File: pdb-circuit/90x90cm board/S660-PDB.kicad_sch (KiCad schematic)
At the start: 45 parts, among them J1 PWR INPUT, J2 PWR OUTPUT, J3 JST-XH 6p to Pi, K1 G2RL-1A DC12, Q2 BC337-40, Q3 2N7000, U1 ATtiny85-20P, U2 LM2936Z-3.3, U3 PC817

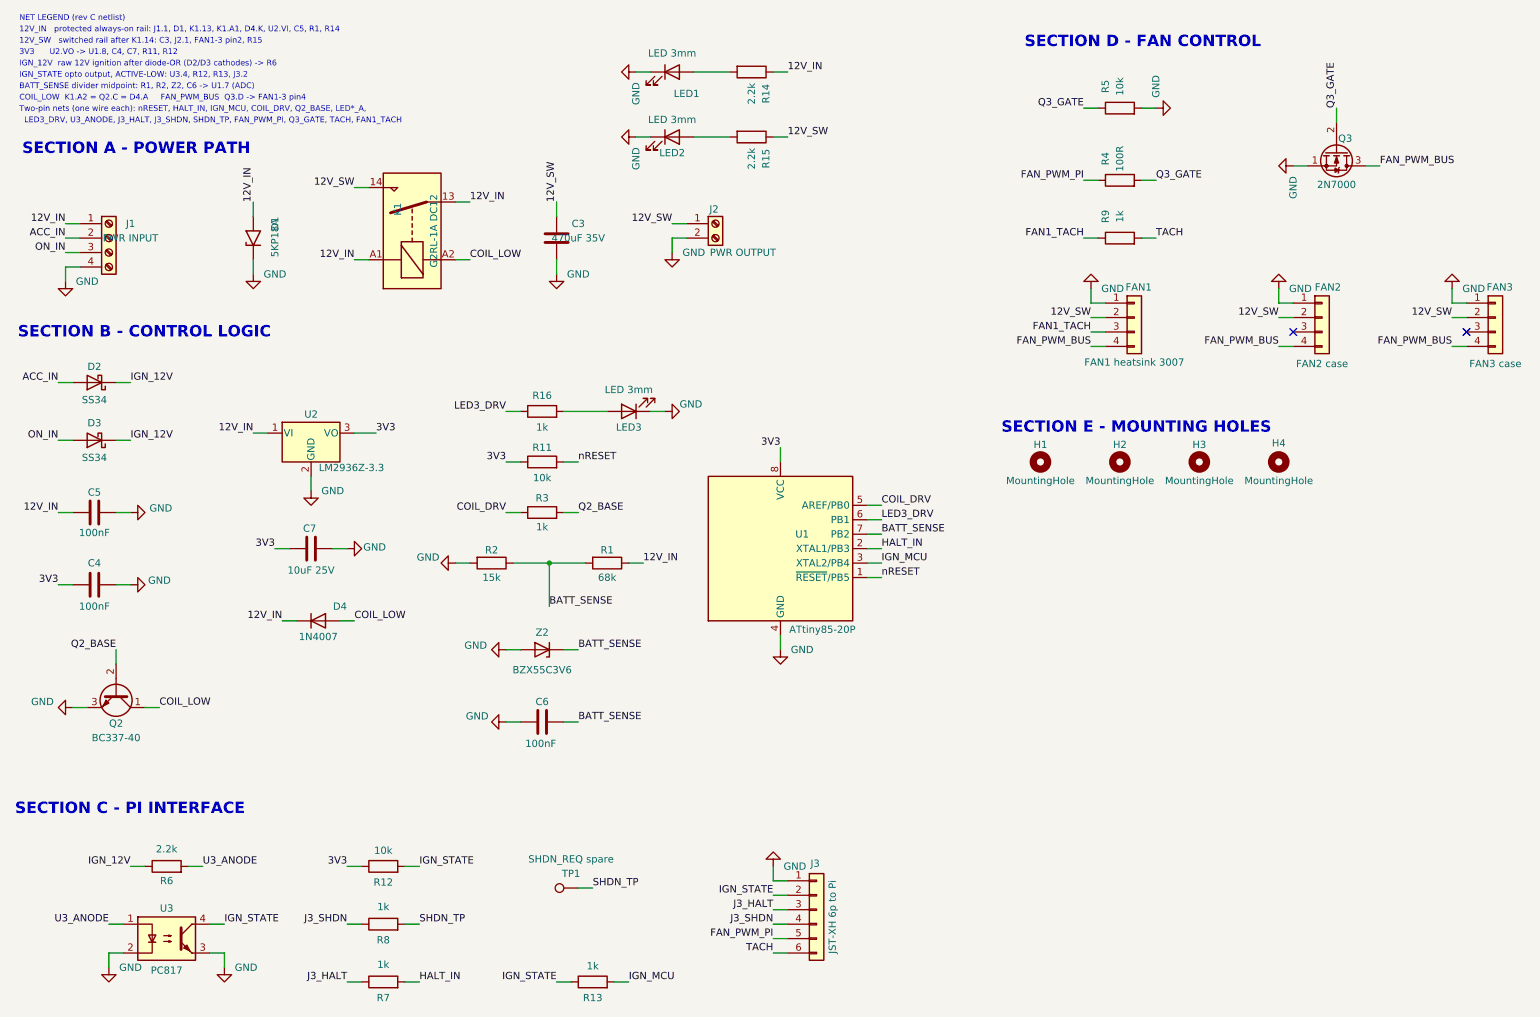
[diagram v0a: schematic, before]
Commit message: PDB rev D: schematic/PCB updates, review notes, BOM/CPL, gerbers and assembly package
Co-Authored-By: Claude Opus 5.5 <noreply@anthropic.com>
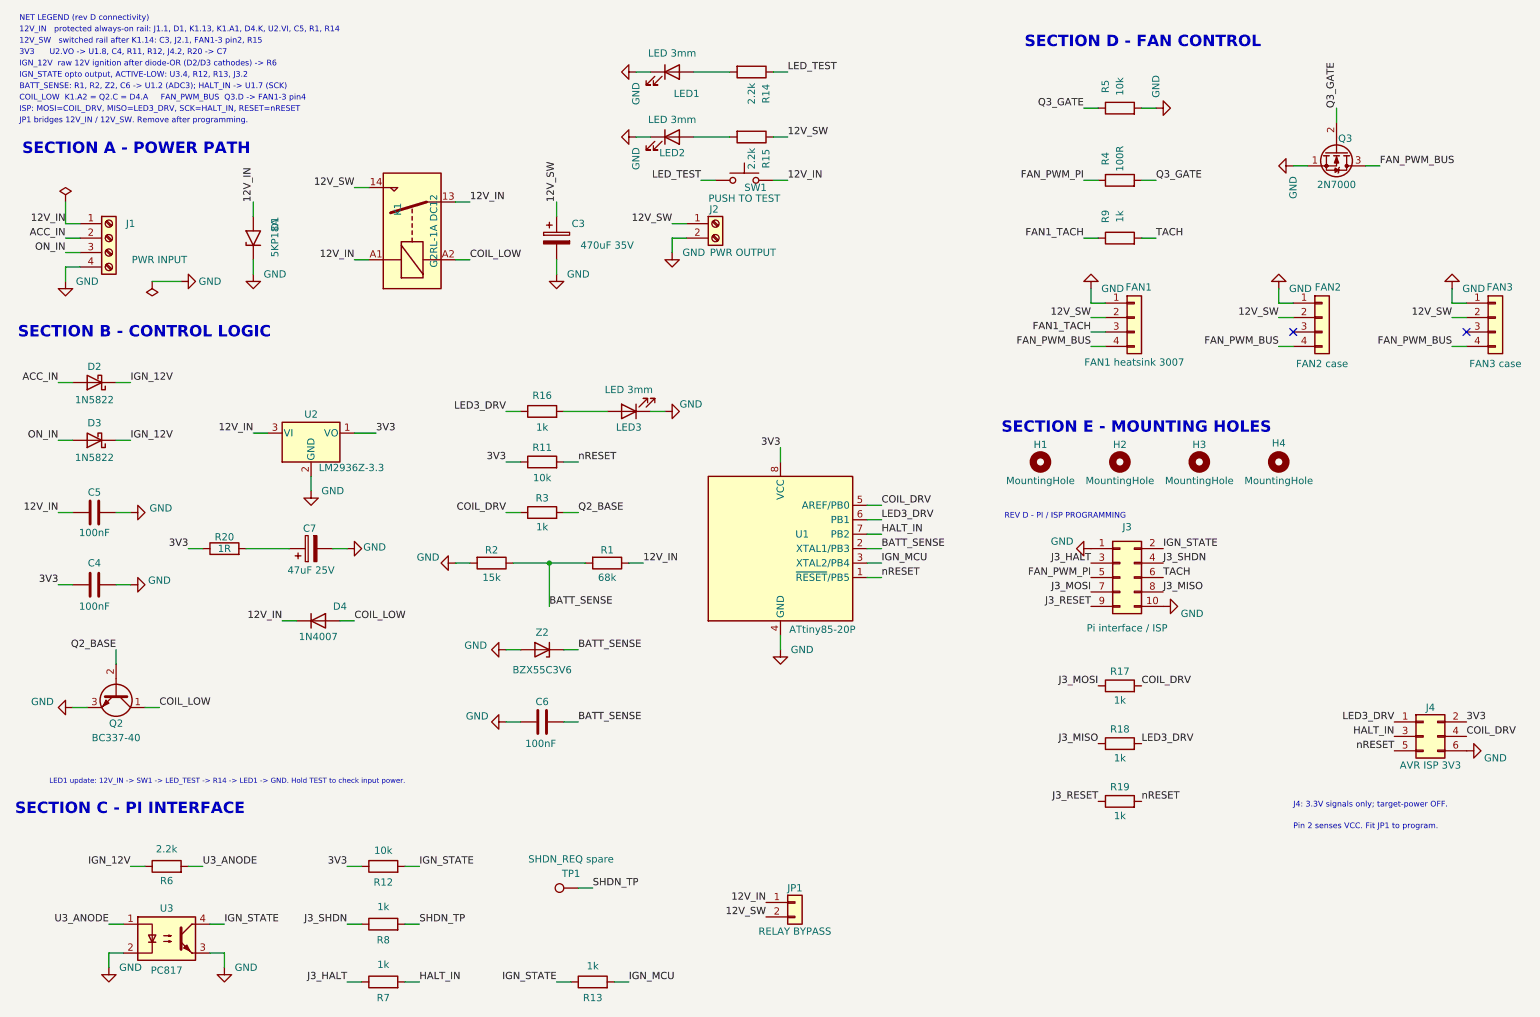
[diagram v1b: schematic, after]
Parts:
- added J4: AVR ISP 3V3, Connector_PinHeader_2.54mm:PinHeader_2x03_P2.54mm_Vertical, symbol Connector_Generic:Conn_02x03_Odd_Even
- added JP1: RELAY BYPASS, S660-PDB:Phoenix_MKDS_1_2_3.5_1751248, symbol Connector_Generic:Conn_01x02
- added R17, R18, R19: 1k, Resistor_THT:R_Axial_DIN0207_L6.3mm_D2.5mm_P10.16mm_Horizontal, symbol Device:R
- added R20: 1R, Resistor_THT:R_Axial_DIN0207_L6.3mm_D2.5mm_P10.16mm_Horizontal, symbol Device:R
- added SW1: PUSH TO TEST, Button_Switch_THT:SW_PUSH_6mm_H4.3mm, symbol Switch:SW_Push
- C3: symbol Device:C -> Device:C_Polarized; Assembly LCSC (none) -> C178715; Assembly MPN (none) -> EEUFR1V471; Assembly Manufacturer (none) -> Panasonic; Assembly Notes (none) -> 10 mm diameter; 5 mm lead pitch. Do not substitute EEUFR1V4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; LCSC (none) -> C178715; MPN (none) -> EEUFR1V471; Manufacturer (none) -> Panasonic
- C4, C5, C6: Assembly LCSC (none) -> C448595; Assembly MPN (none) -> FG28X7R1H104KNT00; Assembly Manufacturer (none) -> TDK; Assembly Notes (none) -> 100 nF 50 V X7R 10%; radial 5 mm pitch.; LCSC (none) -> C448595; MPN (none) -> FG28X7R1H104KNT00; Manufacturer (none) -> TDK
- C7: value 10uF 25V -> 47uF 25V; symbol Device:C -> Device:C_Polarized; Assembly LCSC (none) -> C407893; Assembly MPN (none) -> EEUFR1E470; Assembly Manufacturer (none) -> Panasonic; LCSC (none) -> C407893; MPN (none) -> EEUFR1E470; Manufacturer (none) -> Panasonic; Selection requirement (none) -> EEUFR1E470 with R20=1 ohm in series; validate effective C>=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
- D1: Assembly MPN (none) -> 5KP18A; Assembly Manufacturer (none) -> Diotec Semiconductor; MPN (none) -> 5KP18A; Manufacturer (none) -> Diotec Semiconductor
- D2, D3: value SS34 -> 1N5822; footprint Diode_THT:D_DO-41_SOD81_P10.16mm_Horizontal -> S660-PDB:D_Multicomp_1N5822_DO27_P15.24mm; symbol Diode:SS34 -> Diode:1N5822; Assembly MPN (none) -> 1N5822; Assembly Manufacturer (none) -> Multicomp Pro; Assembly Notes (none) -> Exact Farnell 4050109 DO-27 package; do not substitute DO-2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; Farnell (none) -> 4050109; MPN (none) -> 1N5822; Manufacturer (none) -> Multicomp Pro
- D4: Assembly MPN (none) -> 1N4007-E3/54; Assembly Manufacturer (none) -> Vishay; MPN (none) -> 1N4007-E3/54; Manufacturer (none) -> Vishay
- FAN1, FAN2, FAN3: Assembly MPN (none) -> TSW-104-07-G-S; Assembly Manufacturer (none) -> Samtec; Assembly Notes (none) -> Fit male 1x4 header, not a fan. Verify finished-hole fit wi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; MPN (none) -> TSW-104-07-G-S; Manufacturer (none) -> Samtec
- J1: footprint Connector_Phoenix_MC_HighVoltage:PhoenixContact_MC_1,5_4-GF-5.08_1x04_P5.08mm_Horizontal_ThreadedFlange -> Connector_Phoenix_MC_HighVoltage:PhoenixContact_MC_1,5_4-G-5.08_1x04_P5.08mm_Horizontal; Assembly LCSC (none) -> C5444352; Assembly MPN (none) -> 1836202; Assembly Manufacturer (none) -> Phoenix Contact; Assembly Notes (none) -> PCB header only; mating cable plug not included.; LCSC (none) -> C5444352; MPN (none) -> 1836202; Manufacturer (none) -> Phoenix Contact
- J2: footprint Connector_Phoenix_MC_HighVoltage:PhoenixContact_MC_1,5_2-GF-5.08_1x02_P5.08mm_Horizontal_ThreadedFlange -> Connector_Phoenix_MC_HighVoltage:PhoenixContact_MC_1,5_2-G-5.08_1x02_P5.08mm_Horizontal; Assembly LCSC (none) -> C5355140; Assembly MPN (none) -> 1836189; Assembly Manufacturer (none) -> Phoenix Contact; Assembly Notes (none) -> PCB header only; mating cable plug not included.; LCSC (none) -> C5355140; MPN (none) -> 1836189; Manufacturer (none) -> Phoenix Contact
- J3: value JST-XH 6p to Pi -> Pi interface / ISP; footprint Connector_JST:JST_XH_B6B-XH-A_1x06_P2.50mm_Vertical -> Connector_PinHeader_2.54mm:PinHeader_2x05_P2.54mm_Vertical; symbol Connector_Generic:Conn_01x06 -> Connector_Generic:Conn_02x05_Odd_Even; Assembly MPN (none) -> TSW-105-07-G-D; Assembly Manufacturer (none) -> Samtec; Assembly Notes (none) -> Male 2x5 header; verify finished-hole fit with assembler.; MPN (none) -> TSW-105-07-G-D; Manufacturer (none) -> Samtec
- K1: Assembly LCSC (none) -> C1524657; Assembly MPN (none) -> G2RL-1A DC12; Assembly Manufacturer (none) -> Omron; LCSC (none) -> C1524657; MPN (none) -> G2RL-1A DC12; Manufacturer (none) -> Omron
- LED1, LED2, LED3: Assembly MPN (none) -> WP3A8ID; Assembly Manufacturer (none) -> Kingbright; Assembly Notes (none) -> Red 3 mm LED; pad 1 cathode.; MPN (none) -> WP3A8ID; Manufacturer (none) -> Kingbright
- Q2: footprint Package_TO_SOT_THT:TO-92_Inline -> Package_TO_SOT_THT:TO-92_Inline_Wide; Assembly MPN (none) -> BC337-40; Assembly Manufacturer (none) -> Diotec Semiconductor; Assembly Notes (none) -> Pads 1 C, 2 B, 3 E. 2.54 mm pitch; confirm lead forming.; MPN (none) -> BC337-40; Manufacturer (none) -> Diotec Semiconductor
- Q3: footprint Package_TO_SOT_THT:TO-92_Inline -> Package_TO_SOT_THT:TO-92_Inline_Wide; Assembly MPN (none) -> 2N7000; Assembly Manufacturer (none) -> Diotec Semiconductor; Assembly Notes (none) -> Pads 1 S, 2 G, 3 D. 2.54 mm pitch.; MPN (none) -> 2N7000; Manufacturer (none) -> Diotec Semiconductor
- R1: Assembly MPN (none) -> MFR-25FBF52-68K; Assembly Manufacturer (none) -> Yageo; Assembly Notes (none) -> 1%, 0.25 W; form axial leads to 10.16 mm.; MPN (none) -> MFR-25FBF52-68K; Manufacturer (none) -> Yageo
- R11, R12, R5: Assembly LCSC (none) -> C1519255; Assembly MPN (none) -> MFR-25FBF52-10K; Assembly Manufacturer (none) -> Yageo; Assembly Notes (none) -> 1%, 0.25 W; form axial leads to 10.16 mm.; LCSC (none) -> C1519255; MPN (none) -> MFR-25FBF52-10K; Manufacturer (none) -> Yageo
- R13, R16, R3, R7, R8, R9: Assembly LCSC (none) -> C1364484; Assembly MPN (none) -> MFR-25FBF52-1K; Assembly Manufacturer (none) -> Yageo; Assembly Notes (none) -> 1%, 0.25 W; form axial leads to 10.16 mm.; LCSC (none) -> C1364484; MPN (none) -> MFR-25FBF52-1K; Manufacturer (none) -> Yageo
- R14, R15, R6: Assembly MPN (none) -> MFR-25FBF52-2K2; Assembly Manufacturer (none) -> Yageo; Assembly Notes (none) -> 1%, 0.25 W; form axial leads to 10.16 mm.; MPN (none) -> MFR-25FBF52-2K2; Manufacturer (none) -> Yageo
- R2: Assembly LCSC (none) -> C3556390; Assembly MPN (none) -> MFR-25FBF52-15K; Assembly Manufacturer (none) -> Yageo; Assembly Notes (none) -> 1%, 0.25 W; form axial leads to 10.16 mm.; LCSC (none) -> C3556390; MPN (none) -> MFR-25FBF52-15K; Manufacturer (none) -> Yageo
- R4: Assembly MPN (none) -> MFR-25FBF52-100R; Assembly Manufacturer (none) -> Yageo; Assembly Notes (none) -> 1%, 0.25 W; form axial leads to 10.16 mm.; MPN (none) -> MFR-25FBF52-100R; Manufacturer (none) -> Yageo
- U1: Assembly LCSC (none) -> C3170386; Assembly MPN (none) -> A 08-LC-TT; Assembly Manufacturer (none) -> ASSMANN WSW Components; Assembly Notes (none) -> ASSEMBLY OVERRIDE: fit socket only; owner inserts ATtiny85.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; LCSC (none) -> C965497; MPN (none) -> ATTINY85-20PU; Manufacturer (none) -> Microchip; Socket Datasheet (none) -> https://www.assmann-wsw.com/uploads/datasheets/ASS_0810_CO.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
- U2: footprint Package_TO_SOT_THT:TO-92_Inline -> Package_TO_SOT_THT:TO-92_Inline_Wide; symbol Regulator_Linear:LM2936-3.3 -> Regulator_Linear:LM2936-3.3_TO92; Assembly MPN (none) -> LM2936Z-3.3/NOPB; Assembly Manufacturer (none) -> Texas Instruments; Assembly Notes (none) -> 3.3 V variant only; pads 1 OUT, 2 GND, 3 IN. Form leads to 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; MPN (none) -> LM2936Z-3.3/NOPB; Manufacturer (none) -> Texas Instruments
- U3: Assembly MPN (none) -> ISP817X; Assembly Manufacturer (none) -> Isocom Components; Assembly Notes (none) -> DIP-4 7.62 mm; pads 1 A, 2 K, 3 E, 4 C.; MPN (none) -> ISP817X; Manufacturer (none) -> Isocom Components
- Z2: Assembly MPN (none) -> BZX55C3V6-TAP; Assembly Manufacturer (none) -> Vishay; MPN (none) -> BZX55C3V6-TAP; Manufacturer (none) -> Vishay
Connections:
- net 12V_IN: now also U2.3 (VI), JP1.1 (Pin_1), SW1.2; no longer R14.1, U2.1 (VI)
- net 12V_SW: now also JP1.2 (Pin_2)
- net 3V3: now also U2.1 (VO), J4.2 (Pin_2), R20.1; no longer C7.1, U2.3 (VO)
- net BATT_SENSE: now also U1.2 (XTAL1/PB3); no longer U1.7 (PB2)
- net COIL_DRV: now also J4.4 (Pin_4), R17.2
- net GND: now also J3.10 (Pin_10), J4.6 (Pin_6)
- net HALT_IN: now also U1.7 (PB2), J4.3 (Pin_3); no longer U1.2 (XTAL1/PB3)
- net LED3_DRV: now also J4.1 (Pin_1), R18.2
- net nRESET: now also J4.5 (Pin_5), R19.2
- new net: C7.1, R20.2
- new net J3_MISO: J3.8 (Pin_8), R18.1
- new net J3_MOSI: J3.7 (Pin_7), R17.1
- new net J3_RESET: J3.9 (Pin_9), R19.1
- new net LED_TEST: R14.1, SW1.1
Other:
- note added: "3V3 U2.VO -> U1.8, C4, R11, R12, J4.2, R20 -> C7"
- note added: "BATT_SENSE: R1, R2, Z2, C6 -> U1.2 (ADC3); HALT_IN -> U1.7 (SCK)"
- note added: "ISP: MOSI=COIL_DRV, MISO=LED3_DRV, SCK=HALT_IN, RESET=nRESET"
- note added: "J4: 3.3V signals only; target-power OFF."
- note added: "JP1 bridges 12V_IN / 12V_SW. Remove after programming."
- note added: "LED1 update: 12V_IN -> SW1 -> LED_TEST -> R14 -> LED1 -> GND. Hold TEST to check input power."
- note added: "NET LEGEND (rev D connectivity)"
- note added: "Pin 2 senses VCC. Fit JP1 to program."
- note added: "REV D - PI / ISP PROGRAMMING"
- note removed: "3V3 U2.VO -> U1.8, C4, C7, R11, R12"
- note removed: "BATT_SENSE divider midpoint: R1, R2, Z2, C6 -> U1.7 (ADC)"
- note removed: "LED3_DRV, U3_ANODE, J3_HALT, J3_SHDN, SHDN_TP, FAN_PWM_PI, Q3_GATE, TACH, FAN1_TACH"
- note removed: "NET LEGEND (rev C netlist)"
- note removed: "Two-pin nets (one wire each): nRESET, HALT_IN, IGN_MCU, COIL_DRV, Q2_BASE, LED*_A,"
